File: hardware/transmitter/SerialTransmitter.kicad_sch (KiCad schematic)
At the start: 38 parts, among them J1 Conn_01x08_Male, J2 Conn_01x02_Male, J3 Conn_01x03_Male, J4 Conn_01x08_Male, J5 Conn_01x03_Male, J6 Conn_01x04_Male, Q1 2N7000, SW1 SW_DIP_x08, SW2 SW_Push, U1 74LS165, U2 74LS191, U3 74LS74, U4 74LS132, U5 74LS132, U6 74LS244

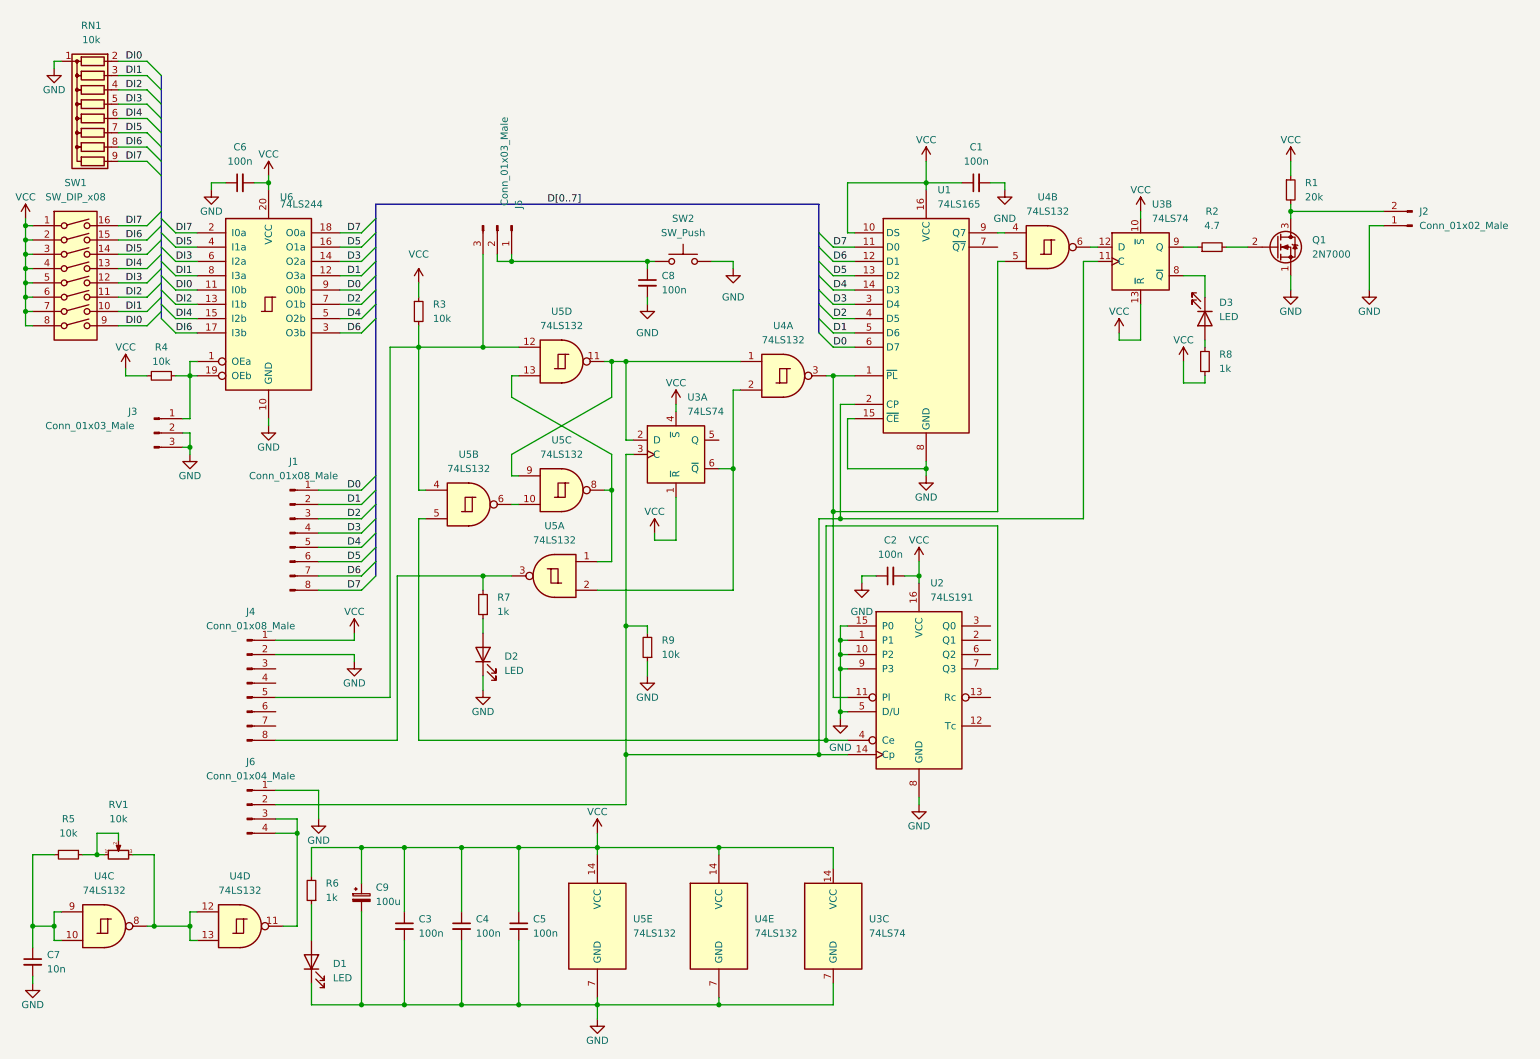
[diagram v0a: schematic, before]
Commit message: Added some notes to the schematic, changed the names of the components, moved some parts.
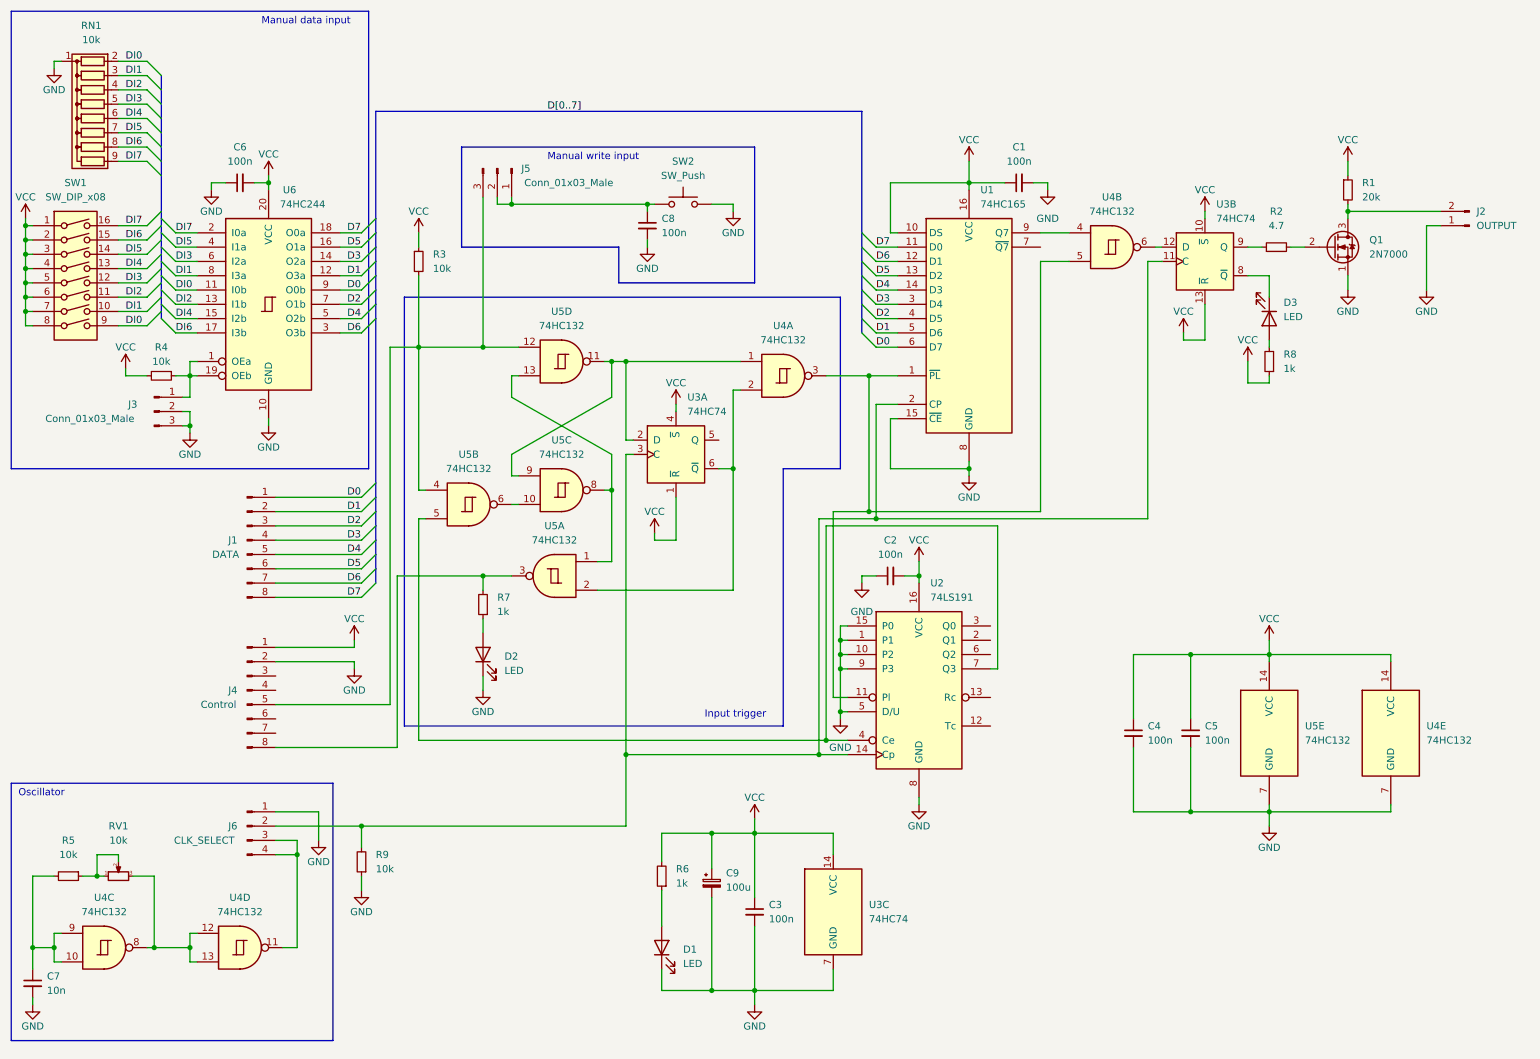
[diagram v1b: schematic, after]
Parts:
- J1: value Conn_01x08_Male -> DATA
- J2: value Conn_01x02_Male -> OUTPUT
- J4: value Conn_01x08_Male -> Control
- J6: value Conn_01x04_Male -> CLK_SELECT
- U1: value 74LS165 -> 74HC165
- U3: value 74LS74 -> 74HC74
- U4, U5: value 74LS132 -> 74HC132
- U6: value 74LS244 -> 74HC244
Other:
- note added: "Input trigger"
- note added: "Manual data input"
- note added: "Manual write input"
- note added: "Oscillator"
- moved on the sheet: C1, C3, C4, C5, C7, C8, C9, D1, D3, J1, J2, J3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
